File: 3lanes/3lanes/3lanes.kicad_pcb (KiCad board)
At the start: 2 copper layers, 32.5 x 144.5 mm, 4 parts, among them J1 Conn_01x18_Female, J2 Conn_01x18_Female, J3 Conn_01x18_Female, J4 Raspberry_Pi_2_3

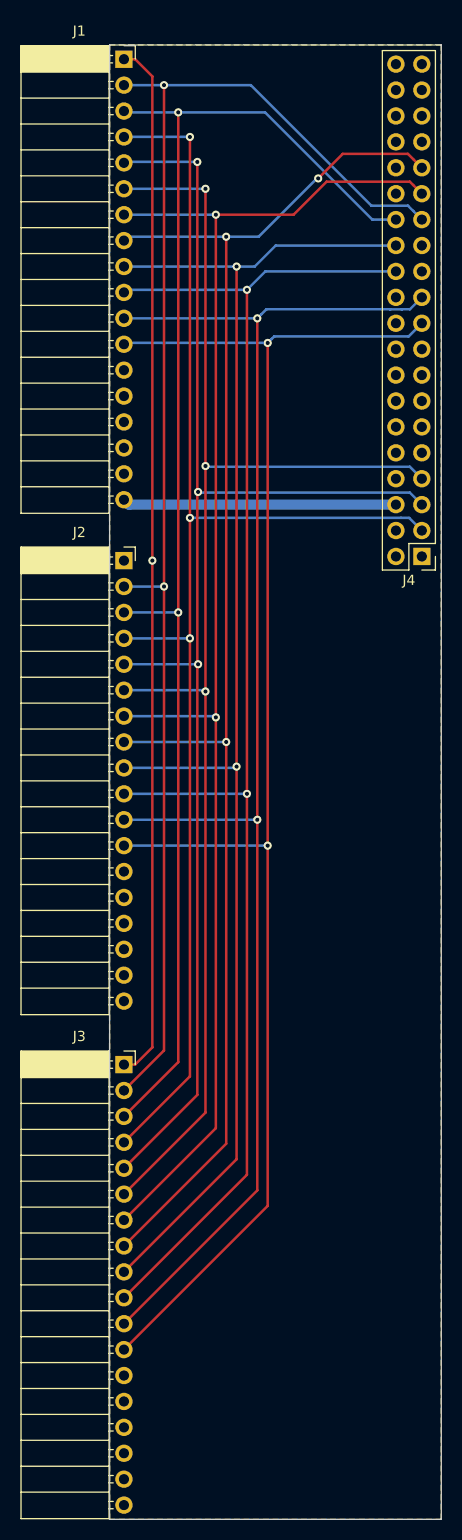
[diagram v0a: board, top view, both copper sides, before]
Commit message: Make PCB connections sturdier by making the PCB extend under the connectors
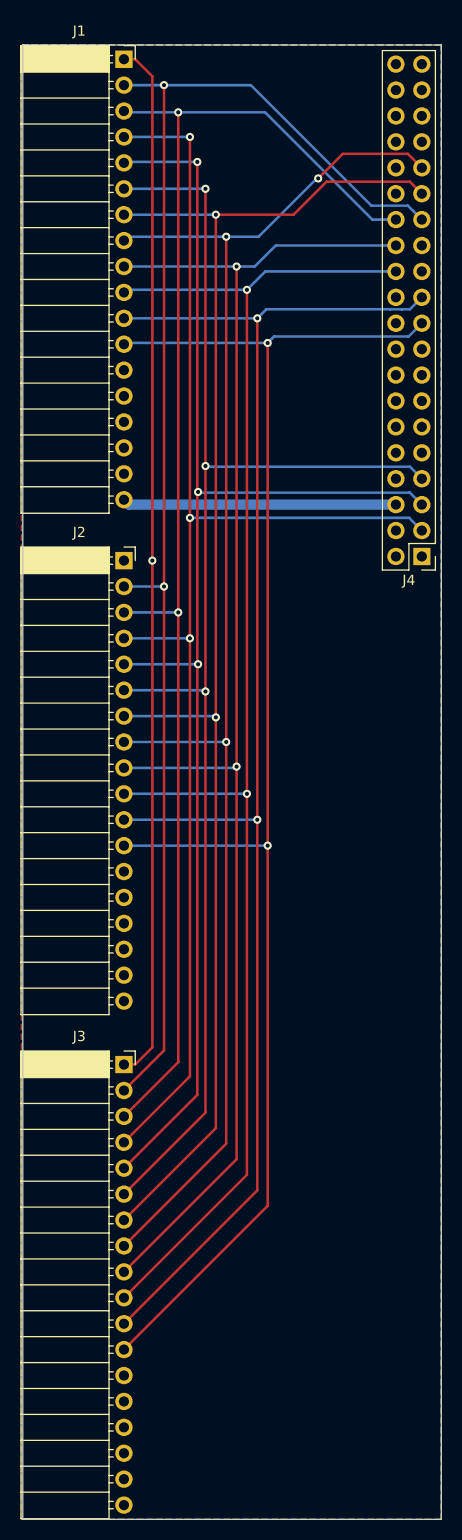
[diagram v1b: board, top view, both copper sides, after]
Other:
- board size 32.5 x 144.5 mm -> 41 x 144.5 mm
